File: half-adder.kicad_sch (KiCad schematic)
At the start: 53 parts, among them J1 A, J2 B, J3 C, J4 OUTPUT, J5 CARRY OUT, Q13 BC547, Q15 BC547, Q2 BC547, Q20 BC547, Q24 BC547, Q7 BC547

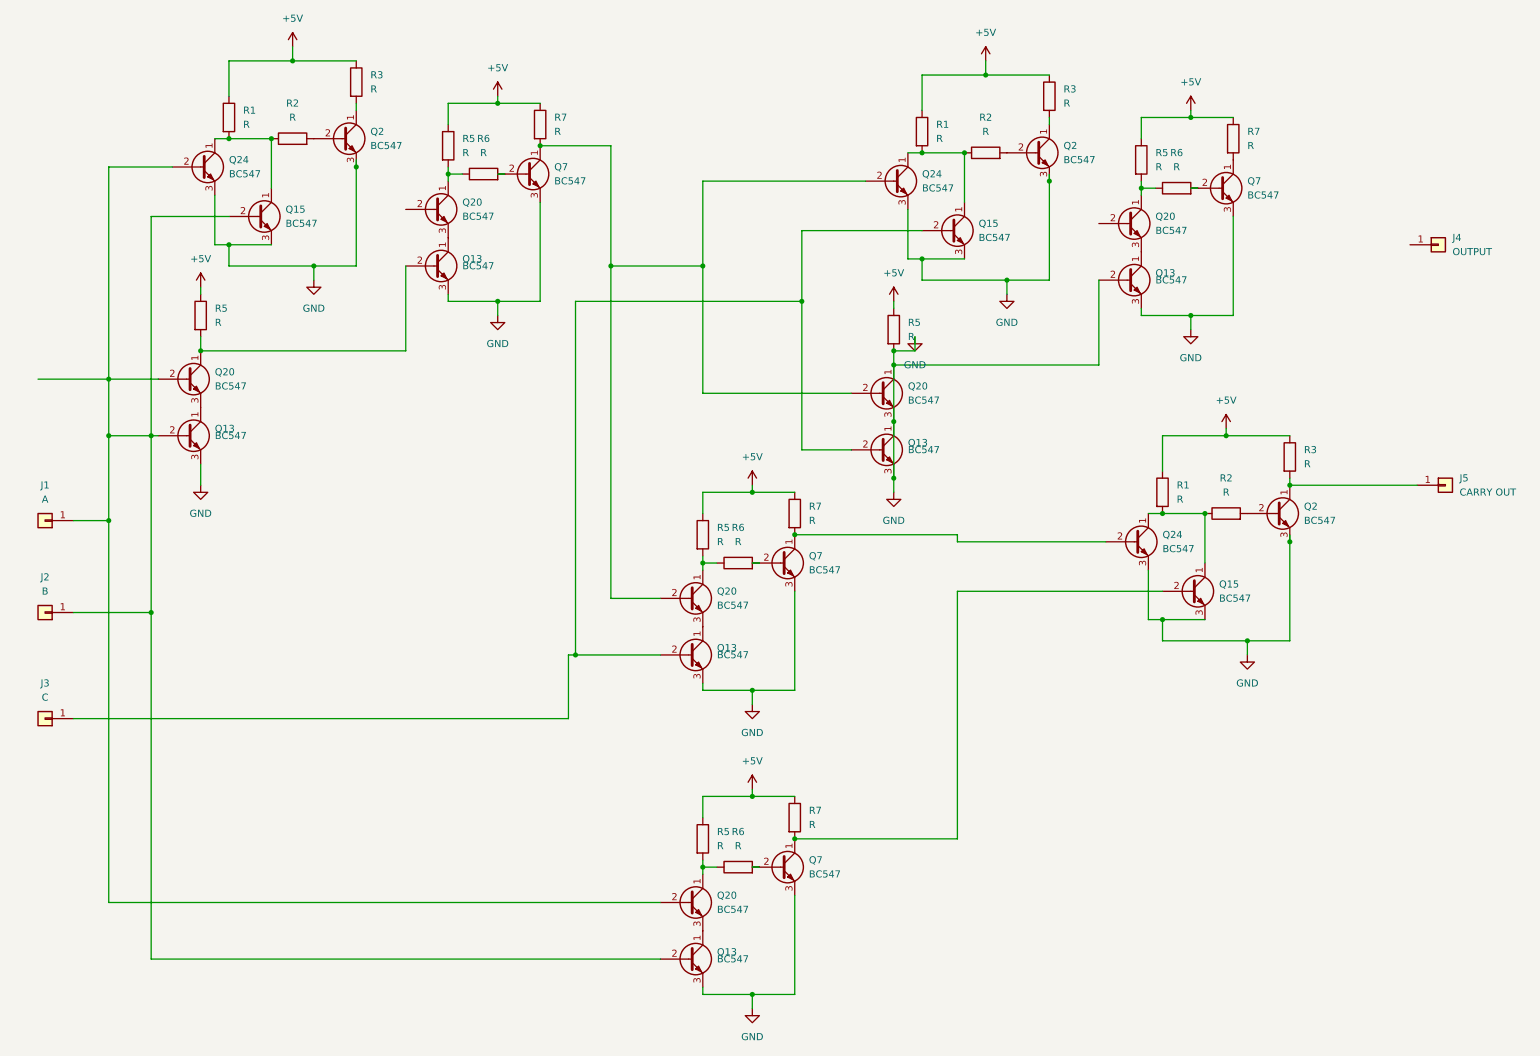
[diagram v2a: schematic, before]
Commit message: Fix design rule checker errors
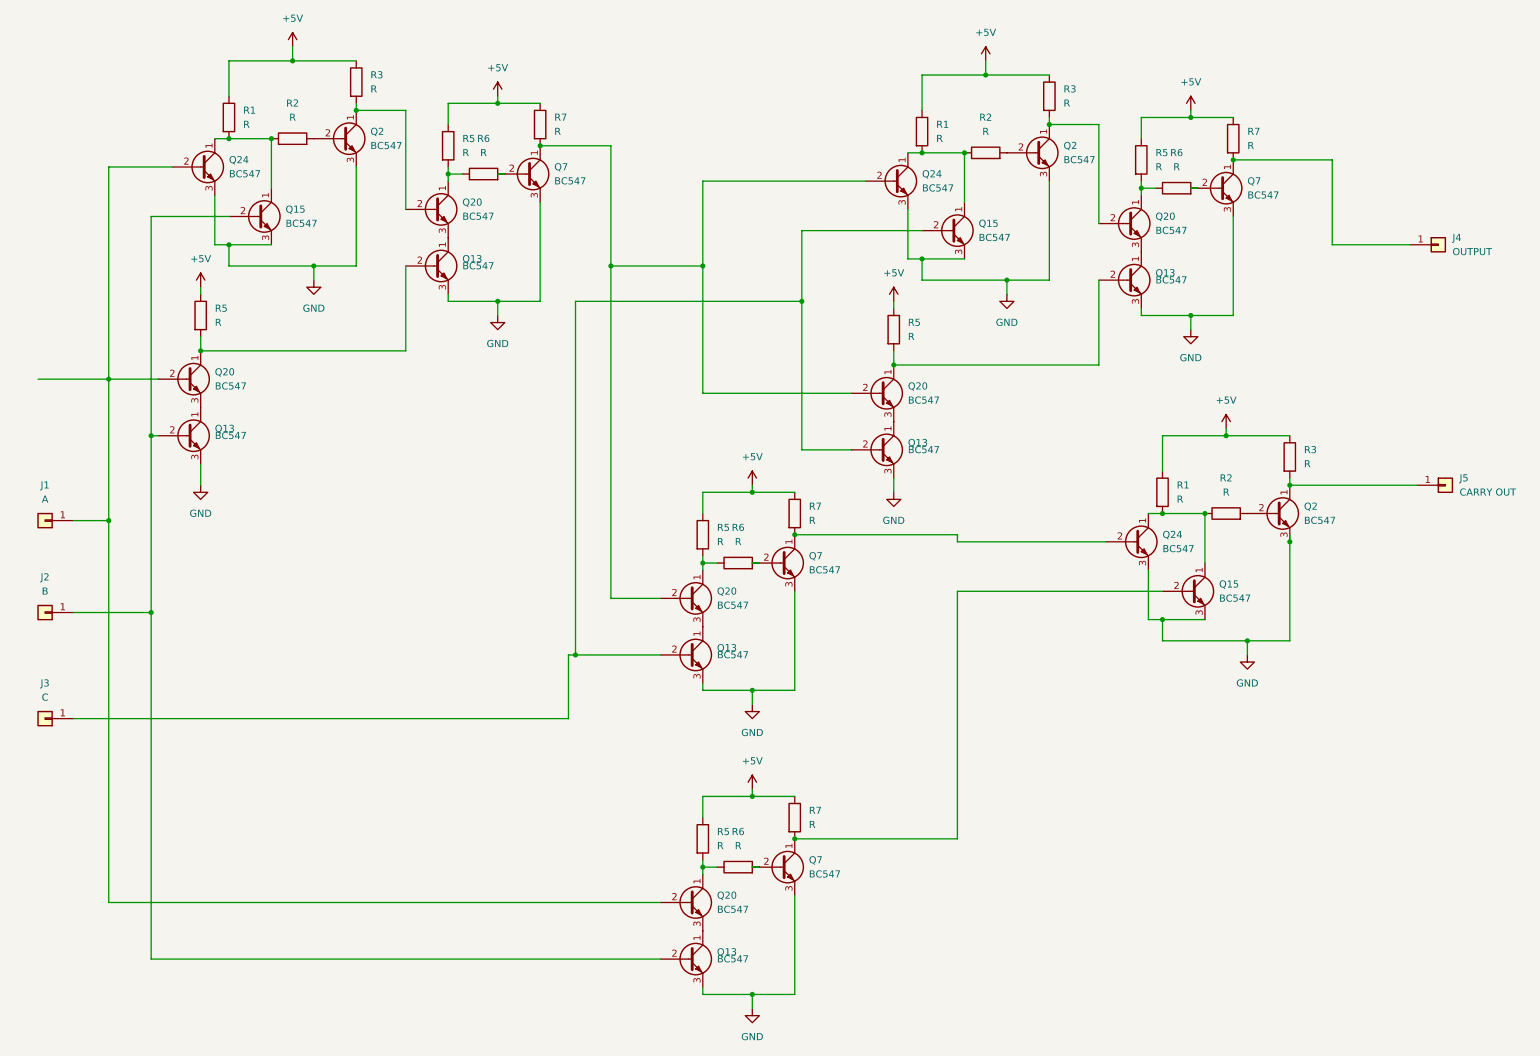
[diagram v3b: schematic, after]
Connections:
- net GND: no longer Q13.1 (C), Q13.2 (B), Q20.1 (C), Q20.3 (E), R5.2
- net at Q2.1 (C), R3.2: now also Q20.2 (B) (x2)
- net at Q7.1 (C), R7.2: now also J4.1 (Pin_1)
- net at J1.1 (Pin_1), Q20.2 (B), Q20.2 (B)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: no longer J2.1 (Pin_1), Q13.2 (B), Q13.2 (B), Q15.2 (B)
- new net: J2.1 (Pin_1), Q13.2 (B), Q13.2 (B), Q15.2 (B)
- new net: Q13.2 (B), Q20.1 (C), R5.2
- new net: Q13.1 (C), Q20.3 (E)
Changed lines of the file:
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@@
   (junction (at 38.1 120.65) (diameter 0) (color 0 0 0 0)
   )
-  (junction (at 199.39 43.18) (diameter 0) (color 0 0 0 0)
+  (junction (at 67.31 58.42) (diameter 0) (color 0 0 0 0)
   )
   (junction (at 153.67 161.29) (diameter 0) (color 0 0 0 0)
@@
   (junction (at 184.15 38.1) (diameter 0) (color 0 0 0 0)
   )
-  (junction (at 171.45 73.66) (diameter 0) (color 0 0 0 0)
-  )
   (junction (at 38.1 88.9) (diameter 0) (color 0 0 0 0)
   )
@@
   (junction (at 120.65 58.42) (diameter 0) (color 0 0 0 0)
   )
+  (junction (at 232.41 39.37) (diameter 0) (color 0 0 0 0)
+  )
   (junction (at 242.57 97.79) (diameter 0) (color 0 0 0 0)
   )
-  (junction (at 74.93 40.64) (diameter 0) (color 0 0 0 0)
-  )
   (junction (at 242.57 107.95) (diameter 0) (color 0 0 0 0)
   )
-  (junction (at 171.45 96.52) (diameter 0) (color 0 0 0 0)
-  )
   (junction (at 91.44 41.91) (diameter 0) (color 0 0 0 0)
   )
@@
   (junction (at 52.07 54.61) (diameter 0) (color 0 0 0 0)
   )
+  (junction (at 74.93 30.48) (diameter 0) (color 0 0 0 0)
+  )
   (junction (at 100.33 29.21) (diameter 0) (color 0 0 0 0)
   )
   (junction (at 219.71 102.87) (diameter 0) (color 0 0 0 0)
   )
-  (junction (at 67.31 58.42) (diameter 0) (color 0 0 0 0)
-  )
   (junction (at 227.33 102.87) (diameter 0) (color 0 0 0 0)
   )
   (junction (at 176.53 38.1) (diameter 0) (color 0 0 0 0)
   )
-  (junction (at 30.48 88.9) (diameter 0) (color 0 0 0 0)
-  )
   (junction (at 107.95 36.83) (diameter 0) (color 0 0 0 0)
   )
@@
   (junction (at 219.71 121.92) (diameter 0) (color 0 0 0 0)
   )
-  (junction (at 171.45 86.36) (diameter 0) (color 0 0 0 0)
-  )
   (junction (at 171.45 76.2) (diameter 0) (color 0 0 0 0)
   )
@@
   (junction (at 52.07 35.56) (diameter 0) (color 0 0 0 0)
   )
+  (junction (at 199.39 33.02) (diameter 0) (color 0 0 0 0)
+  )
   (junction (at 234.95 125.73) (diameter 0) (color 0 0 0 0)
   )
@@
     (stroke (width 0) (type default))
   )
+  (wire (pts (xy 74.93 30.48) (xy 83.82 30.48))
+    (stroke (width 0) (type default))
+  )
   (wire (pts (xy 120.65 118.11) (xy 129.54 118.11))
     (stroke (width 0) (type default))
@@
     (stroke (width 0) (type default))
   )
-  (wire (pts (xy 171.45 96.52) (xy 171.45 86.36))
-    (stroke (width 0) (type default))
-  )
   (wire (pts (xy 137.16 58.42) (xy 137.16 81.28))
     (stroke (width 0) (type default))
@@
     (stroke (width 0) (type default))
   )
-  (wire (pts (xy 30.48 78.74) (xy 30.48 88.9))
-    (stroke (width 0) (type default))
-  )
   (wire (pts (xy 137.16 58.42) (xy 137.16 43.18))
     (stroke (width 0) (type default))
   )
+  (wire (pts (xy 67.31 58.42) (xy 67.31 60.96))
+    (stroke (width 0) (type default))
+  )
   (wire (pts (xy 63.5 21.59) (xy 74.93 21.59))
     (stroke (width 0) (type default))
@@
     (stroke (width 0) (type default))
   )
+  (wire (pts (xy 250.19 54.61) (xy 264.16 54.61))
+    (stroke (width 0) (type default))
+  )
   (wire (pts (xy 242.57 96.52) (xy 242.57 97.79))
     (stroke (width 0) (type default))
@@
     (stroke (width 0) (type default))
   )
-  (wire (pts (xy 175.26 73.66) (xy 175.26 71.12))
-    (stroke (width 0) (type default))
-  )
   (wire (pts (xy 137.16 81.28) (xy 163.83 81.28))
     (stroke (width 0) (type default))
@@
     (stroke (width 0) (type default))
   )
+  (wire (pts (xy 250.19 39.37) (xy 232.41 39.37))
+    (stroke (width 0) (type default))
+  )
   (wire (pts (xy 184.15 38.1) (xy 184.15 46.99))
     (stroke (width 0) (type default))
@@
     (stroke (width 0) (type default))
   )
+  (wire (pts (xy 208.28 33.02) (xy 208.28 50.8))
+    (stroke (width 0) (type default))
+  )
   (wire (pts (xy 46.99 73.66) (xy 83.82 73.66))
     (stroke (width 0) (type default))
@@
     (stroke (width 0) (type default))
   )
-  (wire (pts (xy 67.31 58.42) (xy 67.31 60.96))
-    (stroke (width 0) (type default))
-  )
   (wire (pts (xy 154.94 91.44) (xy 163.83 91.44))
     (stroke (width 0) (type default))
@@
     (stroke (width 0) (type default))
   )
-  (wire (pts (xy 199.39 43.18) (xy 199.39 41.91))
-    (stroke (width 0) (type default))
-  )
   (wire (pts (xy 217.17 113.03) (xy 217.17 121.92))
     (stroke (width 0) (type default))
@@
     (stroke (width 0) (type default))
   )
+  (wire (pts (xy 83.82 30.48) (xy 83.82 48.26))
+    (stroke (width 0) (type default))
+  )
   (wire (pts (xy 38.1 88.9) (xy 39.37 88.9))
     (stroke (width 0) (type default))
@@
     (stroke (width 0) (type default))
   )
+  (wire (pts (xy 182.88 107.95) (xy 209.55 107.95))
+    (stroke (width 0) (type default))
+  )
   (wire (pts (xy 17.78 78.74) (xy 30.48 78.74))
     (stroke (width 0) (type default))
@@
     (stroke (width 0) (type default))
   )
-  (wire (pts (xy 182.88 107.95) (xy 209.55 107.95))
-    (stroke (width 0) (type default))
-  )
   (wire (pts (xy 24.13 104.14) (xy 30.48 104.14))
     (stroke (width 0) (type default))
   )
+  (wire (pts (xy 182.88 116.84) (xy 219.71 116.84))
+    (stroke (width 0) (type default))
+  )
   (wire (pts (xy 219.71 125.73) (xy 234.95 125.73))
     (stroke (width 0) (type default))
@@
     (stroke (width 0) (type default))
   )
-  (wire (pts (xy 74.93 58.42) (xy 74.93 40.64))
-    (stroke (width 0) (type default))
-  )
   (wire (pts (xy 217.17 102.87) (xy 219.71 102.87))
     (stroke (width 0) (type default))
   )
+  (wire (pts (xy 250.19 54.61) (xy 250.19 39.37))
+    (stroke (width 0) (type default))
+  )
+  (wire (pts (xy 199.39 33.02) (xy 208.28 33.02))
+    (stroke (width 0) (type default))
+  )
   (wire (pts (xy 154.94 64.77) (xy 154.94 91.44))
     (stroke (width 0) (type default))
@@
     (stroke (width 0) (type default))
   )
-  (wire (pts (xy 182.88 116.84) (xy 219.71 116.84))
-    (stroke (width 0) (type default))
-  )
   (wire (pts (xy 38.1 88.9) (xy 38.1 120.65))
     (stroke (width 0) (type default))
@@
     (stroke (width 0) (type default))
   )
-  (wire (pts (xy 171.45 86.36) (xy 171.45 76.2))
-    (stroke (width 0) (type default))
-  )
   (wire (pts (xy 91.44 64.77) (xy 100.33 64.77))
     (stroke (width 0) (type default))
@@
     (stroke (width 0) (type default))
   )
-  (wire (pts (xy 30.48 88.9) (xy 38.1 88.9))
-    (stroke (width 0) (type default))
-  )
-  (wire (pts (xy 171.45 73.66) (xy 175.26 73.66))
-    (stroke (width 0) (type default))
-  )
   (wire (pts (xy 199.39 31.75) (xy 199.39 33.02))
     (stroke (width 0) (type default))
@@
     (stroke (width 0) (type default))
   )
-  (wire (pts (xy 30.48 88.9) (xy 30.48 104.14))
+  (wire (pts (xy 30.48 78.74) (xy 30.48 104.14))
     (stroke (width 0) (type default))
   )
@@
     (stroke (width 0) (type default))
   )
-  (wire (pts (xy 74.93 40.64) (xy 74.93 39.37))
+  (wire (pts (xy 74.93 40.64) (xy 74.93 58.42))
     (stroke (width 0) (type default))
   )
@@
         )
       )
-    )
-  )
-  (symbol (lib_id "power:GND") (at 175.26 71.12 0) (unit 1)
-    (in_bom yes) (on_board yes) (dnp no) (fields_autoplaced)
-    (property "Reference" "#PWR06" (at 175.26 77.47 0)
-      (effects (font (size 1.27 1.27)) hide)
-    )
-    (property "Value" "GND" (at 175.26 76.2 0)
-      (effects (font (size 1.27 1.27)))
-    )
-    (property "Footprint" "" (at 175.26 71.12 0)
-      (effects (font (size 1.27 1.27)) hide)
-    )
-    (property "Datasheet" "" (at 175.26 71.12 0)
-      (effects (font (size 1.27 1.27)) hide)
-    )
-    (pin "1")
-    (instances
-      (project "and-gate"
-        (path "/3a921072-4f94-44ca-811b-6c49e6e7df63"
-          (reference "#PWR06") (unit 1)
-        )
-      )
-      (project "half-adder"
-        (path "/88c27409-0a88-4cf1-8b65-cf7271709e32"
-          (reference "#PWR014") (unit 1)
-        )
-      )

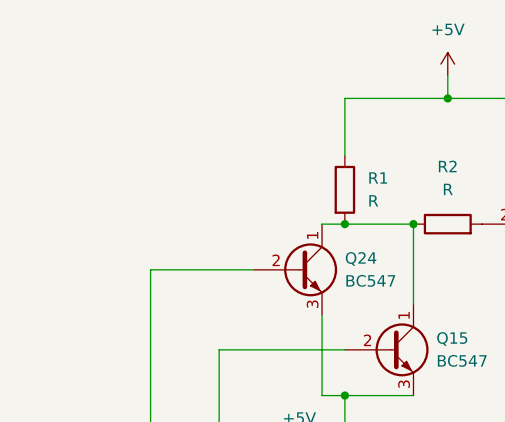
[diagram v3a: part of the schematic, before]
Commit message: Change resistors to more common type
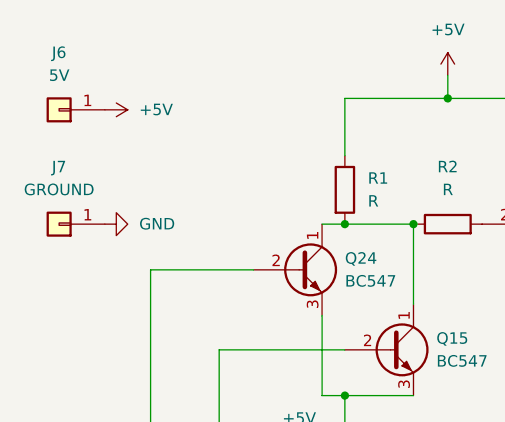
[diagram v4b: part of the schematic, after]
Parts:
- added J6: 5V, Connector_PinHeader_2.54mm:PinHeader_1x01_P2.54mm_Vertical, symbol Connector_Generic:Conn_01x01
- added J7: GROUND, Connector_PinHeader_2.54mm:PinHeader_1x01_P2.54mm_Vertical, symbol Connector_Generic:Conn_01x01
- R1, R2, R3, R5, R6, R7: footprint Resistor_SMD:R_0201_0603Metric -> Resistor_THT:R_Axial_DIN0207_L6.3mm_D2.5mm_P10.16mm_Horizontal
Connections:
- net +5V: now also J6.1 (Pin_1)
- net GND: now also J7.1 (Pin_1)
